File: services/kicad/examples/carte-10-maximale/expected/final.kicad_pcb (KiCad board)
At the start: 6 copper layers, 60.9 x 45.7 mm, 70 parts, among them J1 IN_5V, J10 IO0, J11 IO1, J12 IO2, J13 IO3, J14 IO4, J2 SWD, U1 STM32F103C8T6, U2 AMS1117-3.3

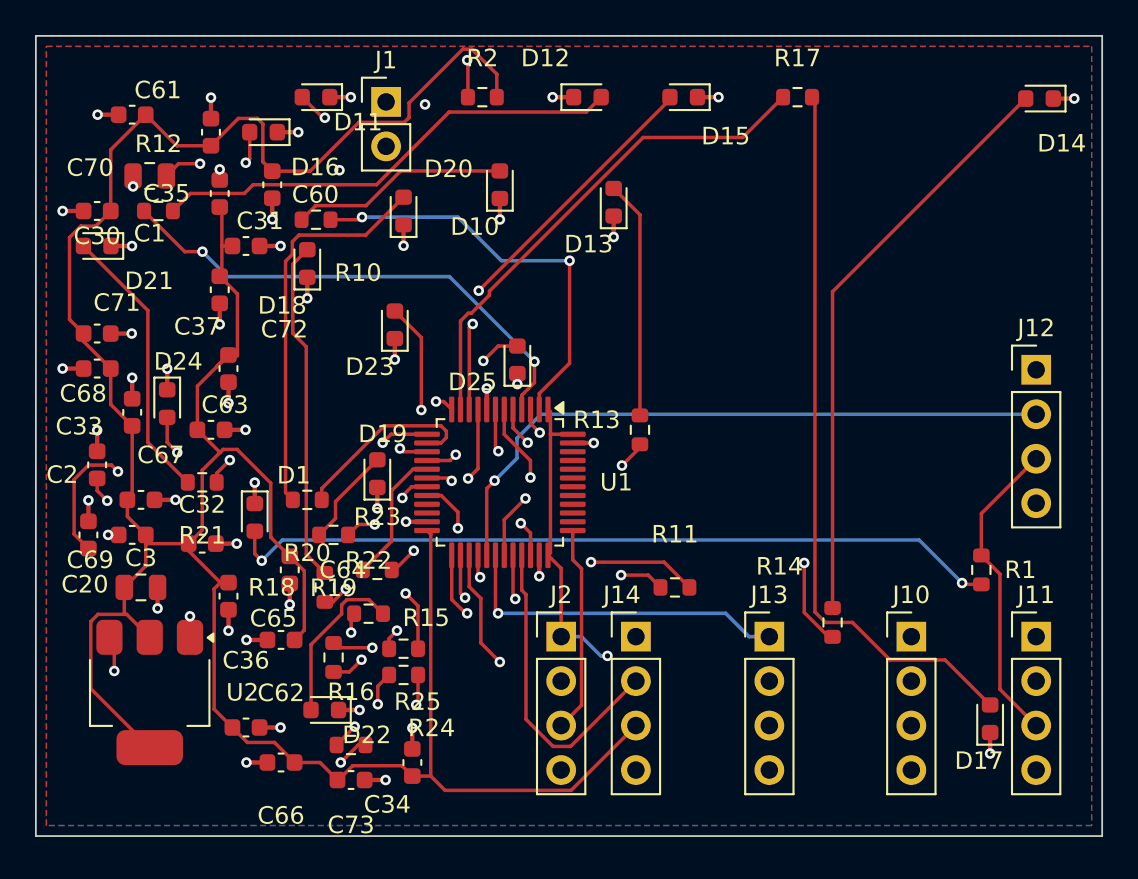
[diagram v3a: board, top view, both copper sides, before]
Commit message: fix(kicad): plan de masse referme — banc DIX cartes sur dix, 0 erreur 0 manquante (#237)
* docs(kicad): la derniere rupture de plan tient a UN segment, pas a un faisceau

Diagnostic complet du seul defaut restant du banc (carte-10), mesure sur le
board qui le porte vraiment, apres consultation de Codex et de GLM.

Mesures sur `/tmp/livr/carte-10-maximale/route.kicad_pcb` (33 violations,
0 erreur, 1 connexion manquante) :

- 23 ilots GND sur les deux faces, exactement 2 orphelins, et ce sont des
  JUMEAUX : F.Cu 1,30 mm2 (porte la pastille C35.2) et B.Cu 0,99 mm2.
- AUCUN de leurs points n a le plan principal en vis-a-vis : ils se font face
  l un l autre. La piste « changer de face par un via », proposee par GLM, est
  donc REFUTEE par la mesure.
- La couture de production visite les deux ilots et refuse la totalite de
  leurs sites (23 et 18 candidats ; obstacle 16/10, hors_polygone 6/7,
  trou_trop_pres 1/1) : un via ne tient pas dans un millimetre carre.
  Le raccord par courte piste rend relies 0, sans_chemin 19.
- Mais le plan principal n est qu a 0,862 mm sur F.Cu et 0,781 mm sur B.Cu, et
  UN SEUL segment coupe le couloir de chaque face (EXT2_1, EXT4_1).

Le plan de Codex — deplacer l obstacle au lieu de chercher un passage a
travers — a donc ici un ensemble a arracher d UN segment par face, pas une
recherche ouverte. Decision de strategie de routage : D-2026-09-22-a, EN
ATTENTE. Rien n est implemente.

Levier natif verifie et jamais appele : LocalRerouter.reroute_segment() de
kicad-tools, utilise par drc/repair_clearance.py, zero appelant Cirqix. Il
travaille sur le document S-expression quand notre code travaille sur pcbnew.

Lecons inscrites dans CLAUDE.md :
- j ai d abord mesure le board VERSIONNE du 21, qui est propre (non_connectes
  0) et se pretait a toutes les demonstrations — un via y tenait avec 0,29 mm
  de marge. Verifier que l artefact PORTE le defaut avant de le diagnostiquer.
- ma premiere sonde raisonnait zone par zone, alors que la carte por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
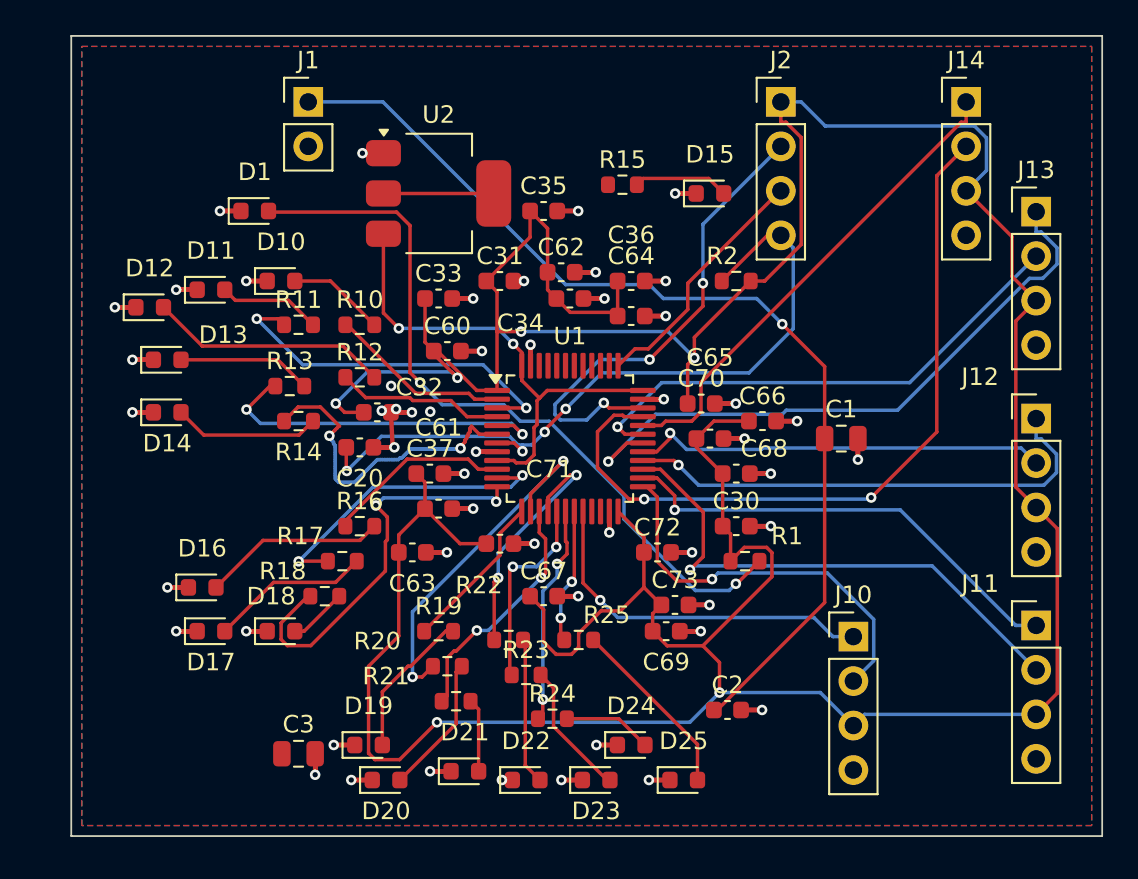
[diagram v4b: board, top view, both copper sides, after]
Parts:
- moved D14 52.9 mm to (86.0, 74.0), turned to 0 degrees
- moved D17 44.8 mm to (88.5, 86.5), turned to 0 degrees
- moved C1 42.3 mm to (124.5, 75.5), turned to 0 degrees
- moved C30 40.7 mm to (118.5, 80.5), turned to 0 degrees
- moved C2 38.6 mm to (118.0, 91.0), turned to 0 degrees
- moved R17 37.1 mm to (96.0, 82.5)
- moved C68 37.0 mm to (118.5, 77.5), turned to 0 degrees
- moved D21 36.6 mm to (103.0, 94.5), turned to 0 degrees
- moved C70 36.4 mm to (116.5, 73.5), turned to 0 degrees
- moved J14 35.9 mm to (131.6, 56.3)
- moved C66 33.7 mm to (120.0, 74.5), turned to 0 degrees
- moved J2 33.0 mm to (121.0, 56.3)
- moved U2 32.9 mm to (101.5, 61.5), turned to 0 degrees
- moved D24 32.9 mm to (112.5, 93.0), turned to 0 degrees
- moved R14 32.6 mm to (93.5, 74.5), turned to 0 degrees
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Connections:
- C3 pad 1: +3V3 -> Net-(C3-1)
- U1 pad 36: +3V3 -> PWR_FLAG
- U1 pad 48: +3V3 -> PWR_FLAG
- U1 pad 9: IO_L5 -> PWR_FLAG
- U2 pad 2: +3V3 -> Net-(U2-2)
- U2 pad 3: VIN -> PWR_FLAG
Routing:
- net GND: track 55.2 -> 175.9 mm, vias 50 -> 52
- net LEDA5: track 41.8 -> 5.47 mm, vias 2 -> 0
- net NRST: track 77.2 -> 42.8 mm, vias 3 -> 4
- net LEDA1: track 39.8 -> 5.87 mm, vias 2 -> 0
- net LEDA7: track 41.7 -> 9.19 mm
- net LEDA6: track 40.2 -> 10.5 mm, vias 2 -> 0
- net PWR_FLAG: track 0.00 -> 28.2 mm, vias 0 -> 2
- net EXT4_2: track 17.9 -> 43.8 mm, vias 0 -> 2
- net LEDA4: track 33.7 -> 8.41 mm
- net LEDA14: track 27.9 -> 5.08 mm, vias 2 -> 0
- net IO_L6: track 33.2 -> 10.7 mm, vias 2 -> 0
- net IO_L2: track 28.9 -> 9.59 mm, vias 2 -> 0
- net IO_L5: track 18.5 -> 0.00 mm, vias 2 -> 0
- net EXT4_1: track 10.3 -> 27.8 mm, vias 1 -> 0
- net EXT3_1: track 19.4 -> 36.4 mm
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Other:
- board size 60.9 x 45.7 mm -> 58.9 x 45.7 mm
- copper layers 6 -> 2

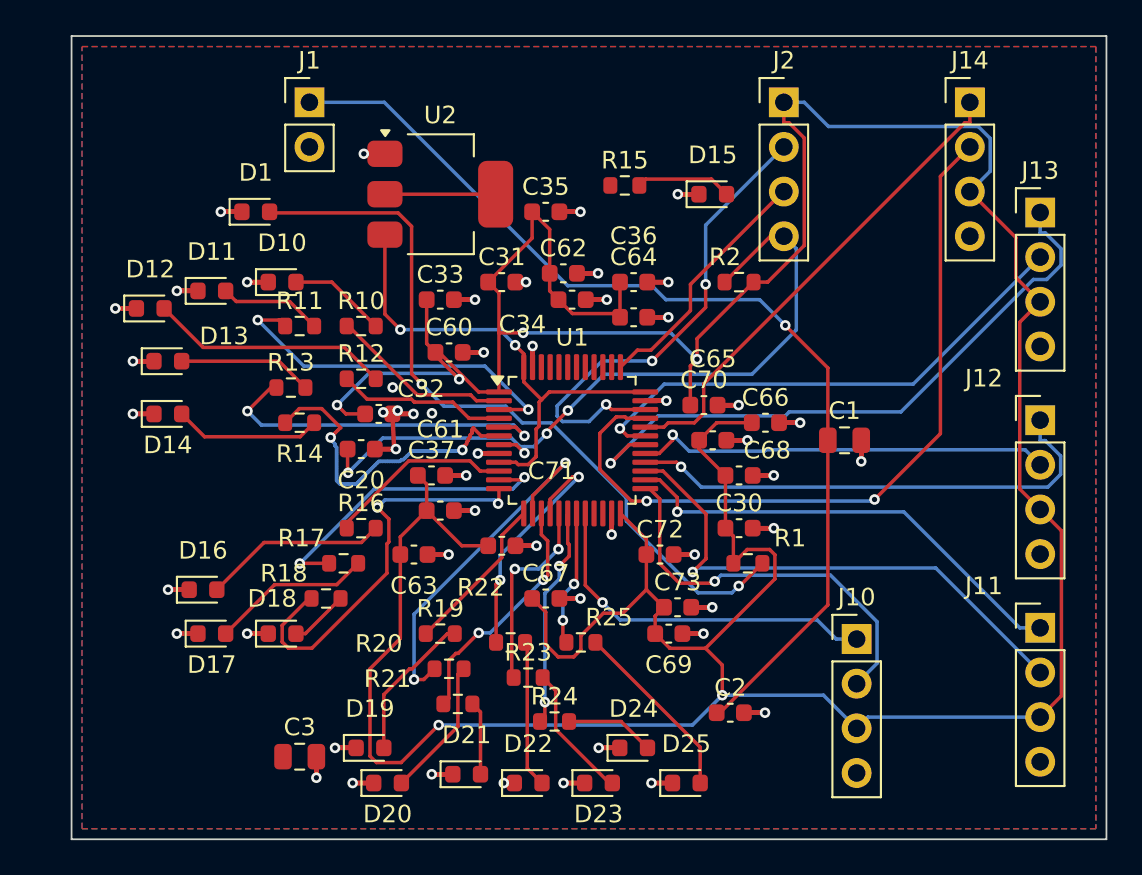
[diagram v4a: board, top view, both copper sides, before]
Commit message: fix(banc): le banc route comme la production — plafond 8, budget du client
D-2026-09-24-f. run_pipeline.py prenait 2 couches et 1800 s par défaut, et
carte-07 écrivait 2 en dur : dix cartes sur quinze ne pouvaient jamais
escalader, et la règle « toute connexion manquante fait monter » était
inerte dans le banc. Mesuré sur carte-07 : 97 %, seule la masse manquante,
« le palier suivant sera tenté »… puis retour à 2 couches.

Plafond par défaut 8 (client Pro Max), budget min(600 + 300 x plafond, 3600)
comme routingSearchBudgetS côté client. En production, rien ne change : le
plafond reste celui du plan.

Livraisons du jour, toutes vérifiées par kicad-cli et contre le schéma
(0 erreur bloquante, 0 connexion manquante, 0 court-circuit) :
carte-04, 05, 06, 08 (campagne de l'après-midi) et carte-09, 10 (4 couches).
Les boards versionnés de ces cartes court-circuitaient des nets du schéma.

Correction de ma propre erreur dans la doc : carte-07 n'avait jamais
escaladé ; les lignes « palier 4 et 6 » du journal étaient celles de
carte-08, démarrée la même minute.

Co-Authored-By: Claude Opus 5.5 <noreply@anthropic.com>
Claude-Session: https://claude.ai/code/session_01TnMqm4La2CxQHHB5K8aSSV
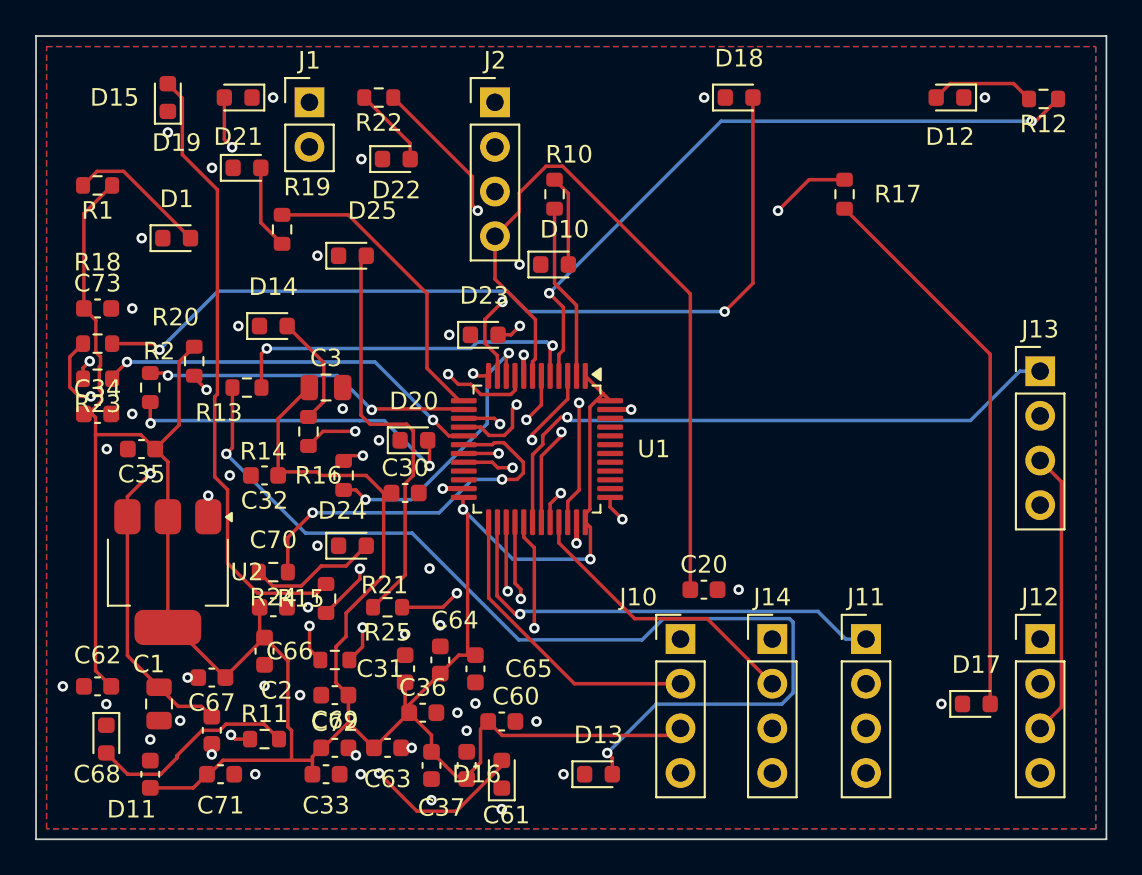
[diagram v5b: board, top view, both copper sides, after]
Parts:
- moved D12 47.1 mm to (130.5, 56.0), turned to 180 degrees
- moved D17 43.7 mm to (132.0, 90.5)
- moved R1 42.8 mm to (82.0, 61.0), turned to 180 degrees
- moved R12 42.0 mm to (135.8, 56.1), turned to 180 degrees
- moved C1 41.8 mm to (85.5, 90.5), turned to -90 degrees
- moved D21 40.6 mm to (90.0, 56.0), turned to 180 degrees
- moved D18 40.1 mm to (118.5, 56.0)
- moved C68 37.6 mm to (85.0, 94.5), turned to 90 degrees
- moved C73 37.1 mm to (82.0, 68.0)
- moved D22 36.3 mm to (99.0, 59.5)
- moved D25 35.5 mm to (96.5, 65.0)
- moved C62 35.4 mm to (82.0, 89.5), turned to 180 degrees
- moved R17 35.4 mm to (124.5, 61.5), turned to -90 degrees
- moved D13 33.9 mm to (110.5, 94.5)
- moved D19 33.7 mm to (90.5, 60.0)
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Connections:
- C3 pad 1: Net-(C3-1) -> +3V3
- U1 pad 36: PWR_FLAG -> +3V3
- U1 pad 48: PWR_FLAG -> +3V3
- U1 pad 9: PWR_FLAG -> IO_L5
- U2 pad 2: Net-(U2-2) -> +3V3
- U2 pad 3: PWR_FLAG -> VIN
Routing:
- net GND: track 175.9 -> 14.4 mm, vias 52 -> 48
- net LEDA3: track 7.66 -> 58.5 mm, vias 0 -> 2
- net LEDA8: track 3.37 -> 49.7 mm, vias 0 -> 2
- net LED_PWR: track 43.4 -> 8.02 mm, vias 2 -> 0
- net LEDA11: track 4.19 -> 35.6 mm, vias 0 -> 2
- net LEDA5: track 5.47 -> 35.3 mm
- net IO_L2: track 9.59 -> 38.7 mm, vias 0 -> 2
- net PWR_FLAG: track 28.2 -> 0.00 mm, vias 2 -> 0
- net EXT4_2: track 43.8 -> 16.6 mm, vias 2 -> 0
- net IO_L5: track 0.00 -> 22.7 mm, vias 0 -> 2
- net LEDA7: track 9.19 -> 31.6 mm
- net LEDA13: track 7.74 -> 29.8 mm, vias 0 -> 2
- net NRST: track 42.8 -> 63.3 mm, vias 4 -> 1
- net LEDA6: track 10.5 -> 28.9 mm, vias 0 -> 2
- net VIN: track 58.1 -> 43.6 mm
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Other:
- board size 58.9 x 45.7 mm -> 60.9 x 45.7 mm
- copper layers 2 -> 4
